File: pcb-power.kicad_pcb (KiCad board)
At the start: 2 copper layers, 53.6 x 53.7 mm, 0 parts

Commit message: pcb design done
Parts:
- added C1: C, Capacitor_THT:CP_Radial_D5.0mm_P2.00mm, B.Cu at (112.0, 76.0)
- added J1: Conn_01x07_Socket, Connector_PinSocket_2.54mm:PinSocket_1x07_P2.54mm_Vertical, F.Cu at (140.0, 80.4)
- added J2: Conn_01x02_Socket, ark:TerminalBlock_bornier-2_P5.08mm, F.Cu at (126.0, 97.0)
- added J3: Conn_01x02_Socket, ark:TerminalBlock_bornier-2_P5.08mm, F.Cu at (126.0, 75.0)
- added Q2: NMOS, Package_TO_SOT_SMD:SOT-23, B.Cu at (100.6, 88.5)
- added Q4: PMOS, Package_TO_SOT_SMD:TO-252-2, B.Cu at (107.5, 99.8)
- added R10: 10k, Resistor_THT:R_Axial_DIN0207_L6.3mm_D2.5mm_P10.16mm_Horizontal, F.Cu at (140.6, 105.5)
- added R4: 20k, Resistor_THT:R_Axial_DIN0207_L6.3mm_D2.5mm_P10.16mm_Horizontal, F.Cu at (147.0, 100.6)
- added R5: 10k, Resistor_THT:R_Axial_DIN0207_L6.3mm_D2.5mm_P10.16mm_Horizontal, F.Cu at (114.0, 99.7)
- added R6: 10k, Resistor_THT:R_Axial_DIN0207_L6.3mm_D2.5mm_P10.16mm_Horizontal, F.Cu at (135.0, 100.6)
- added R7: 10k, Resistor_THT:R_Axial_DIN0207_L6.3mm_D2.5mm_P10.16mm_Horizontal, F.Cu at (143.5, 98.1)
- added R8: 10k, Resistor_THT:R_Axial_DIN0207_L6.3mm_D2.5mm_P10.16mm_Horizontal, F.Cu at (126.6, 104.0)
- added R9: 10k, Resistor_THT:R_Axial_DIN0207_L6.3mm_D2.5mm_P10.16mm_Horizontal, F.Cu at (126.6, 108.0)
- added U1: LM1117DT-5.0, Package_TO_SOT_SMD:TO-252-3_TabPin2, B.Cu at (116.5, 65.5)
- added U2: IRF7303, Package_TO_SOT_SMD:IRF7303, B.Cu at (133.0, 86.0)
- added U3: LM1117DT-5.0, Package_TO_SOT_SMD:TO-252-3_TabPin2, B.Cu at (135.5, 65.7)
- added U4: IRF7104, Package_TO_SOT_SMD:IRF7104, B.Cu at (106.0, 89.0)
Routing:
- net GND: track 0.00 -> 127.9 mm
- net signal: track 0.00 -> 115.7 mm
- net PROBE sec: track 0.00 -> 77.2 mm
- net VCC main: track 0.00 -> 73.6 mm
- net +3.3V: track 0.00 -> 58.7 mm
- net MODE: track 0.00 -> 53.2 mm
- net Net-(U3-VI): track 0.00 -> 49.4 mm
- net Net-(U1-VI): track 0.00 -> 26.7 mm
- net Net-(Q4-D): track 0.00 -> 22.4 mm
- net VCC secondary: track 0.00 -> 21.0 mm
- net PROBE main: track 0.00 -> 18.4 mm
- net Net-(J3-Pin_1): track 0.00 -> 12.1 mm
- net Net-(J2-Pin_1): track 0.00 -> 11.7 mm
- net PYRO 1: track 0.00 -> 4.26 mm
- net PYRO 2: track 0.00 -> 4.26 mm
- added copper zone on B.Cu, net GND

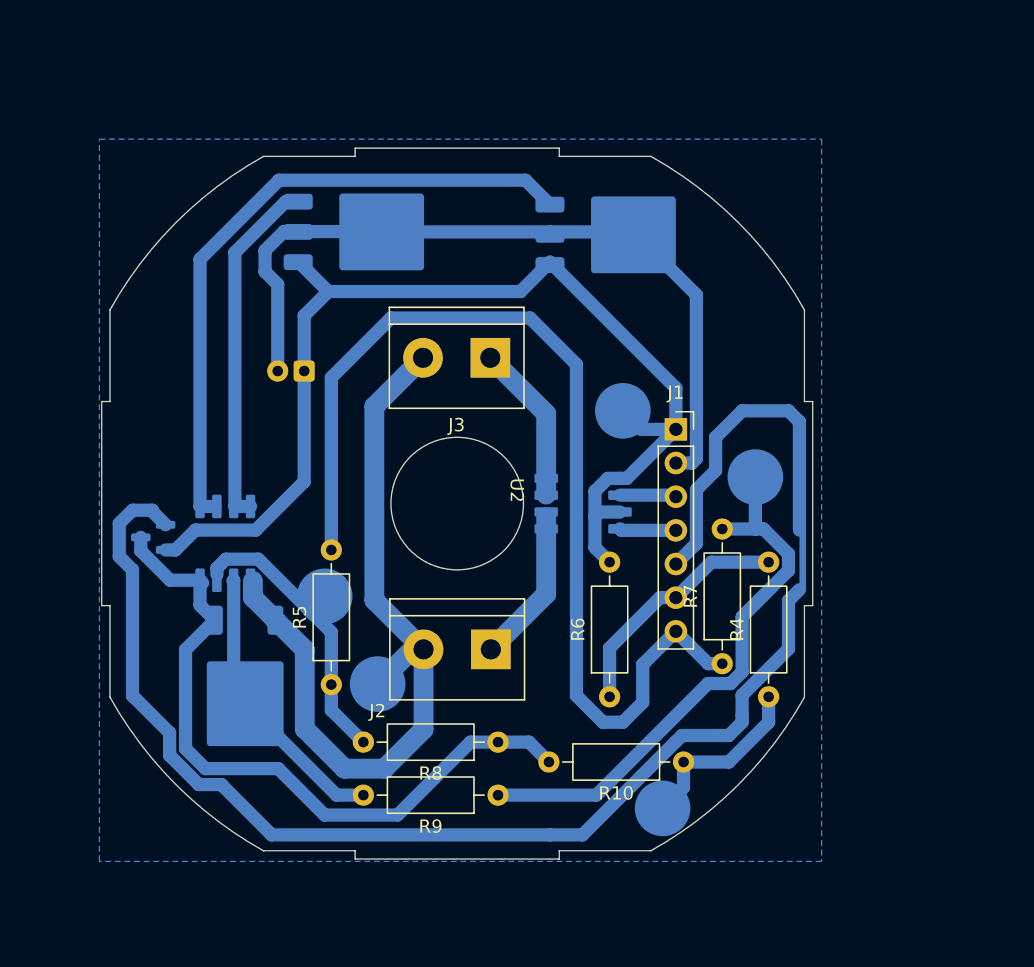
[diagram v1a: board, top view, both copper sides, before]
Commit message: added second layer for connecting batteries
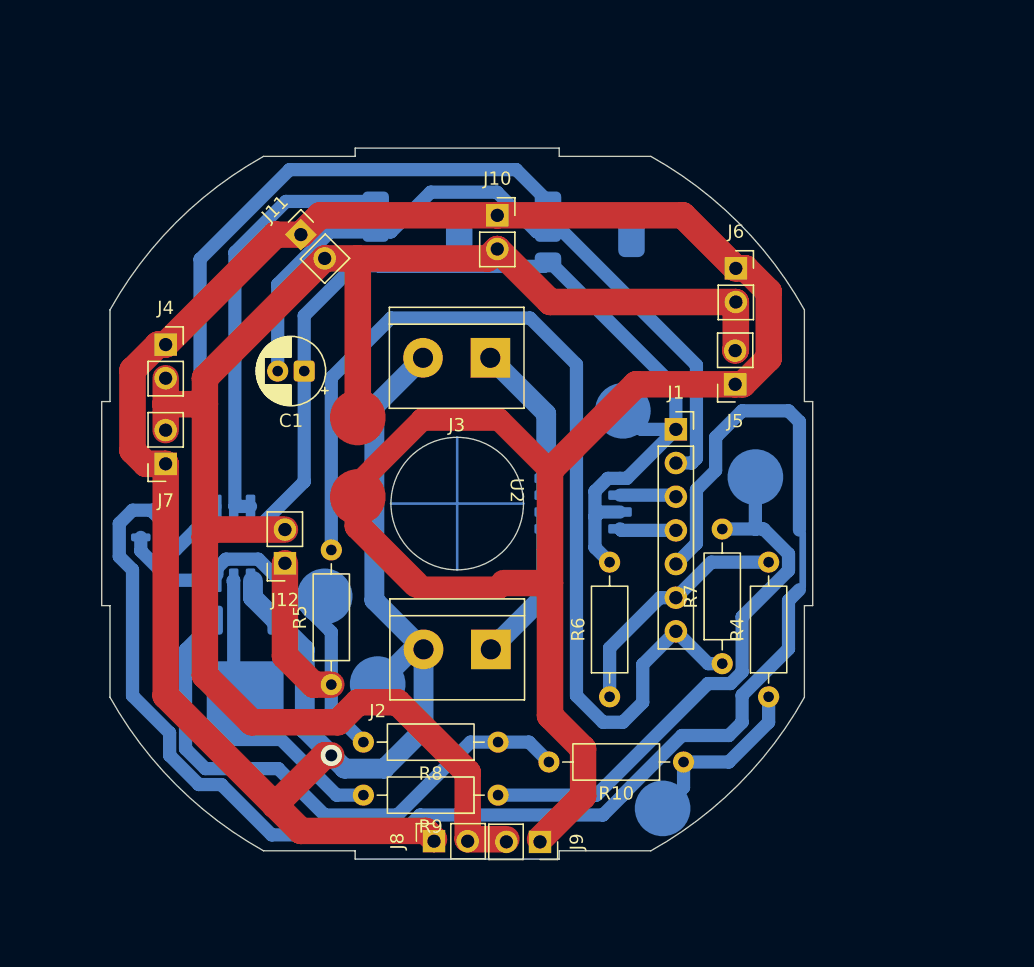
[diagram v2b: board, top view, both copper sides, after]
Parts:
- added J10: Conn_01x02_Socket, Connector_PinSocket_2.54mm:PinSocket_1x02_P2.54mm_Vertical, F.Cu at (126.5, 64.2)
- added J11: Conn_01x02_Socket, Connector_PinSocket_2.54mm:PinSocket_1x02_P2.54mm_Vertical, F.Cu at (111.7, 65.7)
- added J12: Conn_01x02_Socket, Connector_PinSocket_2.54mm:PinSocket_1x02_P2.54mm_Vertical, F.Cu at (110.5, 90.5)
- added J4: Conn_01x02_Socket, Connector_PinSocket_2.54mm:PinSocket_1x02_P2.54mm_Vertical, F.Cu at (101.5, 74.0)
- added J5: Conn_01x02_Socket, Connector_PinSocket_2.54mm:PinSocket_1x02_P2.54mm_Vertical, F.Cu at (144.5, 77.0)
- added J6: Conn_01x02_Socket, Connector_PinSocket_2.54mm:PinSocket_1x02_P2.54mm_Vertical, F.Cu at (144.5, 68.2)
- added J7: Conn_01x02_Socket, Connector_PinSocket_2.54mm:PinSocket_1x02_P2.54mm_Vertical, F.Cu at (101.5, 83.0)
- added J8: Conn_01x02_Socket, Connector_PinSocket_2.54mm:PinSocket_1x02_P2.54mm_Vertical, F.Cu at (121.8, 111.5)
- added J9: Conn_01x02_Socket, Connector_PinSocket_2.54mm:PinSocket_1x02_P2.54mm_Vertical, F.Cu at (129.8, 111.5)
- C1: moved to F.Cu
- U1, U3: footprint Package_TO_SOT_SMD:TO-252-3_TabPin2 -> Package_TO_SOT_SMD:SOT-223
- moved U1 3.96 mm to (120.5, 65.5)
- moved U3 2.05 mm to (133.5, 65.5)
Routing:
- net VCC main: track 73.6 -> 279.0 mm, vias 0 -> 1
- net GND: track 127.9 -> 254.0 mm
- net VCC secondary: track 21.0 -> 32.4 mm
- net Net-(U1-VI): track 26.7 -> 32.6 mm
- net +3.3V: track 58.7 -> 55.2 mm
- removed copper zone on B.Cu, net GND

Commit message: changed Vreg
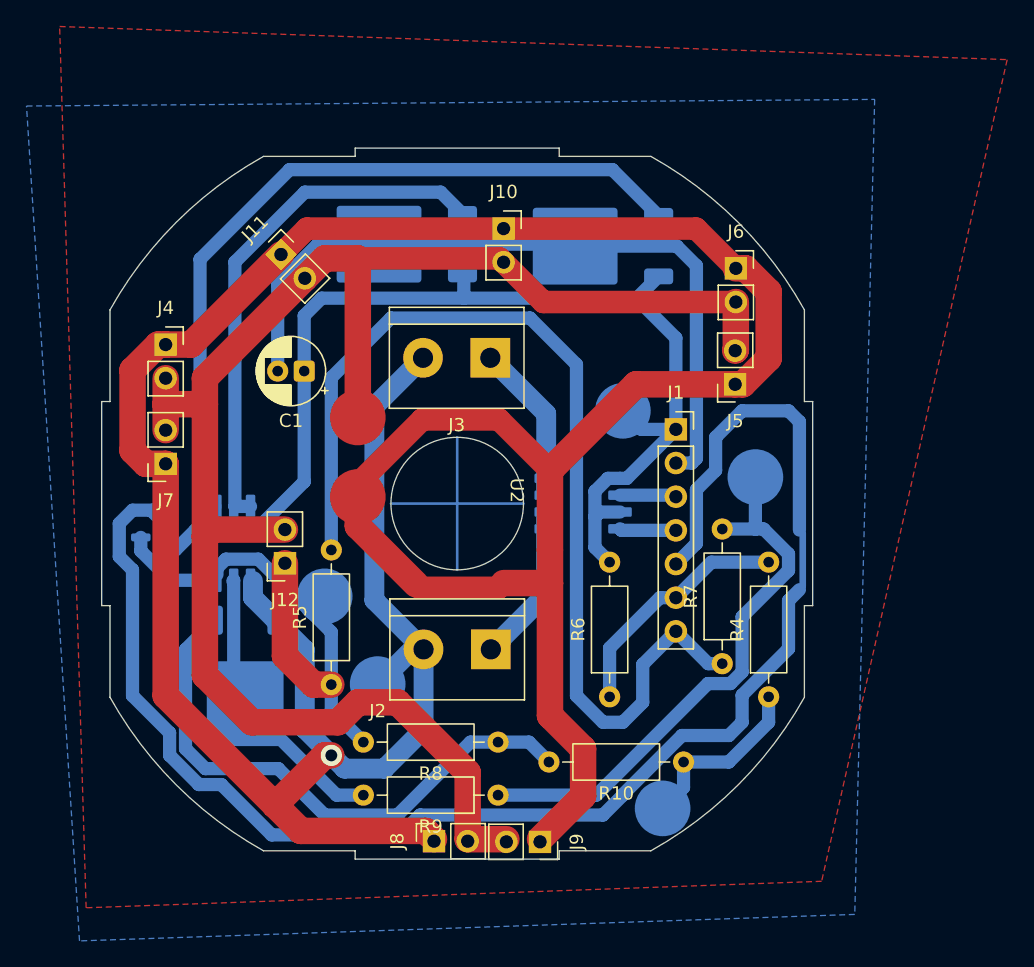
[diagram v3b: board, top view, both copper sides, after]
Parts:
- U1, U3: footprint Package_TO_SOT_SMD:SOT-223 -> Package_TO_SOT_SMD:TO-252-2
- moved J11 2.12 mm to (110.2, 67.2)
- moved U1 1.88 mm to (118.9, 66.4), turned to 180 degrees
- moved J10 1.11 mm to (127.0, 65.2)
- moved U3 1.08 mm to (133.7, 66.6), turned to 180 degrees
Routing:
- net Net-(U3-VI): track 49.8 -> 58.6 mm
- net Net-(U1-VI): track 32.6 -> 39.7 mm
- net GND: track 254.0 -> 257.3 mm
- net +3.3V: track 55.2 -> 56.5 mm
- net VCC main: track 279.0 -> 278.1 mm
- added copper zone on B.Cu, net GND
- added copper zone on F.Cu, net GND

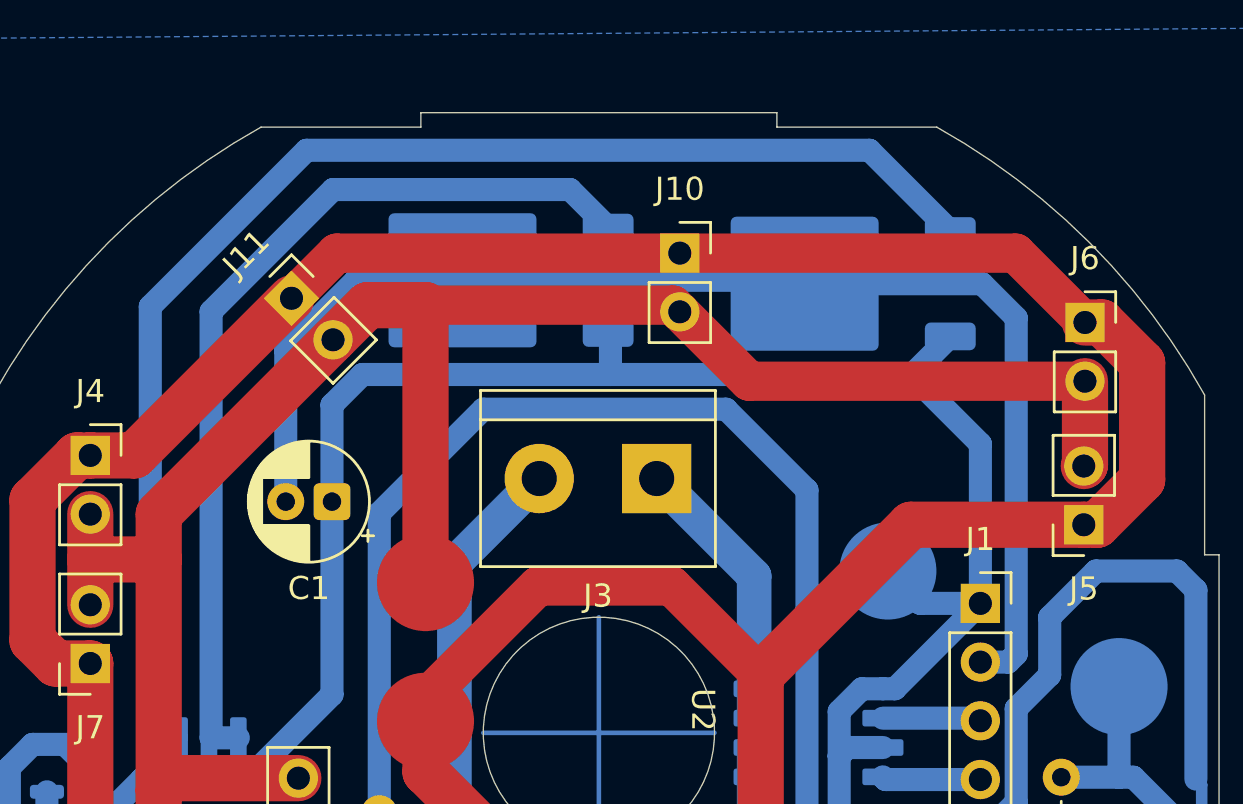
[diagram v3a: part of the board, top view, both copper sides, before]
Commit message: added GND via
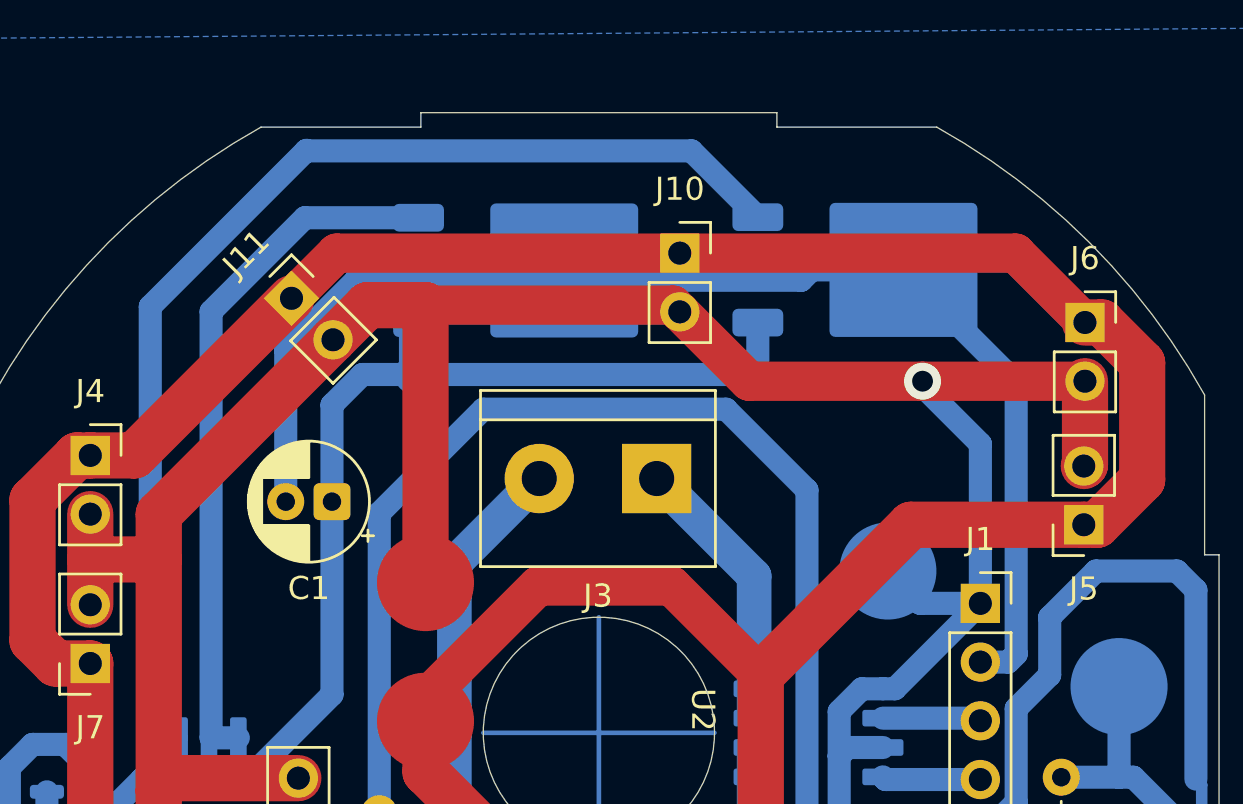
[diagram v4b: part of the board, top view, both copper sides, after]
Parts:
- moved U1 1.93 mm to (120.7, 66.0), turned to 0 degrees
- moved U3 1.85 mm to (135.4, 66.0), turned to 0 degrees
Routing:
- net Net-(U1-VI): track 39.7 -> 30.3 mm
- net Net-(U3-VI): track 58.6 -> 50.1 mm
- net +3.3V: track 56.5 -> 55.0 mm
- net GND: track 257.3 -> 257.8 mm, vias 0 -> 1

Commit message: changed resistor value
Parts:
- R8: value 10k -> 470k
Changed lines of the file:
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@@
 			)
 		)
-		(property "Value" "10k"
+		(property "Value" "470k"
 			(at 5.08 2.37 0)
 			(layer "F.Fab")
